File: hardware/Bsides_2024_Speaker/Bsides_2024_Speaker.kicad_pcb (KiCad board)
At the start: 2 copper layers, 144.4 x 144.3 mm, 40 parts, among them J1 Conn_02x03_Odd_Even, J2 Battery, J3 Battery, J4 OLED, P1 USB_C_Plug_USB2.0, Q1 DMG3415U-7, SW1 ON, SW2 RESET, SW3 BOOT, SW4 RESET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

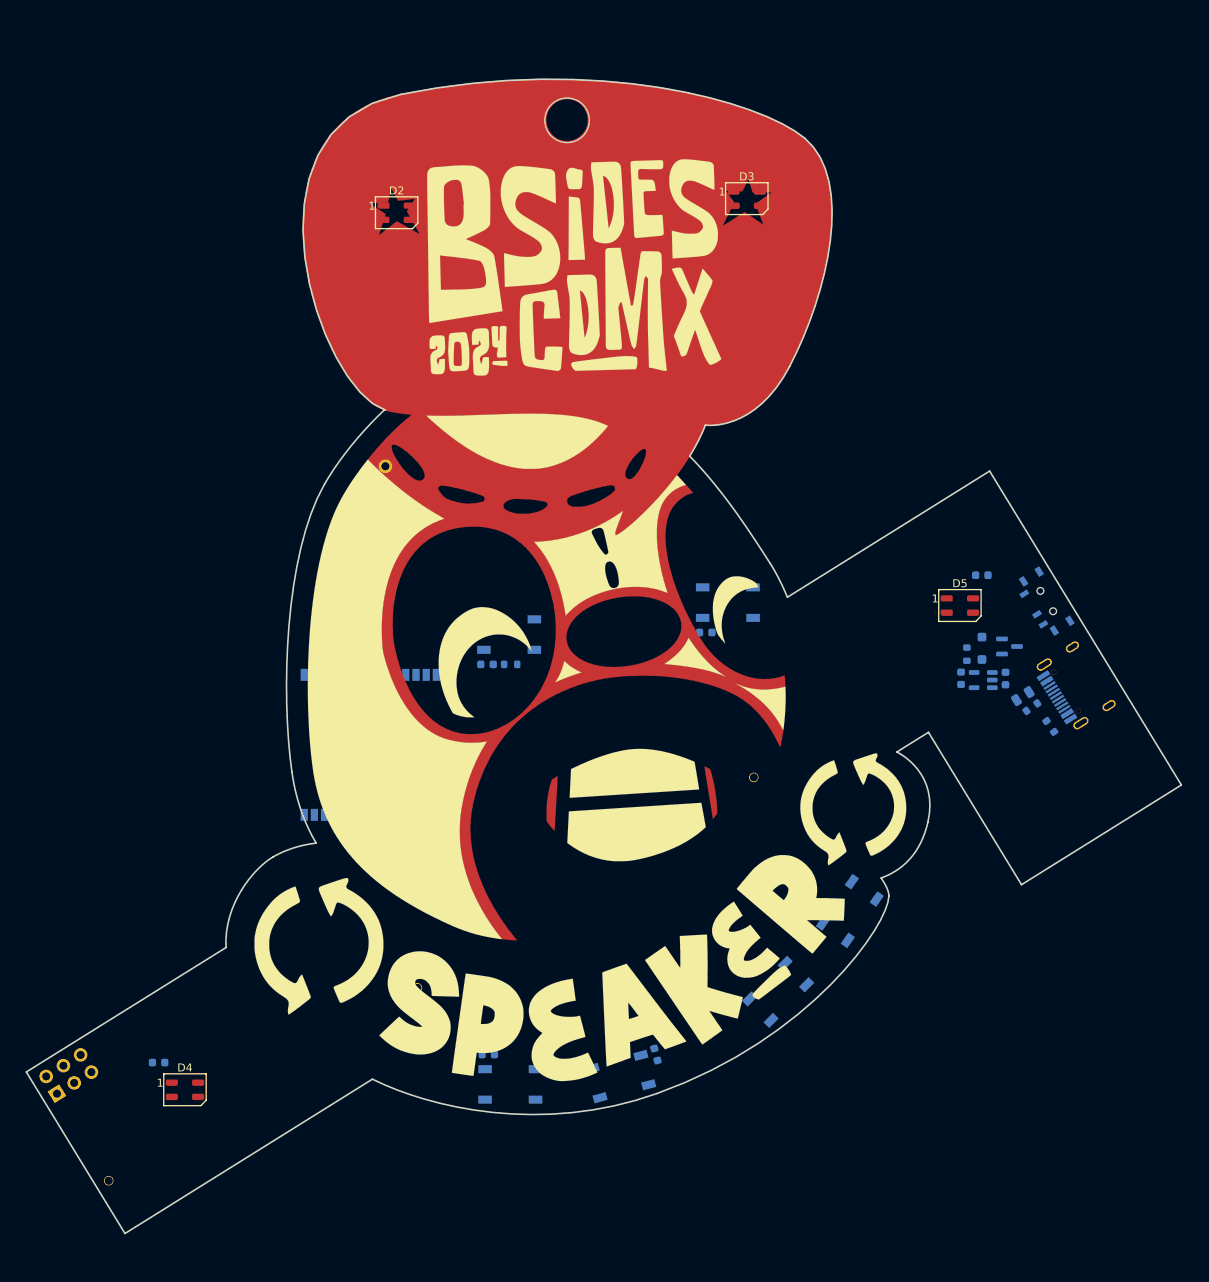
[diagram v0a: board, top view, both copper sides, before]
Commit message: feat(Hw):Update_Route_Speaker
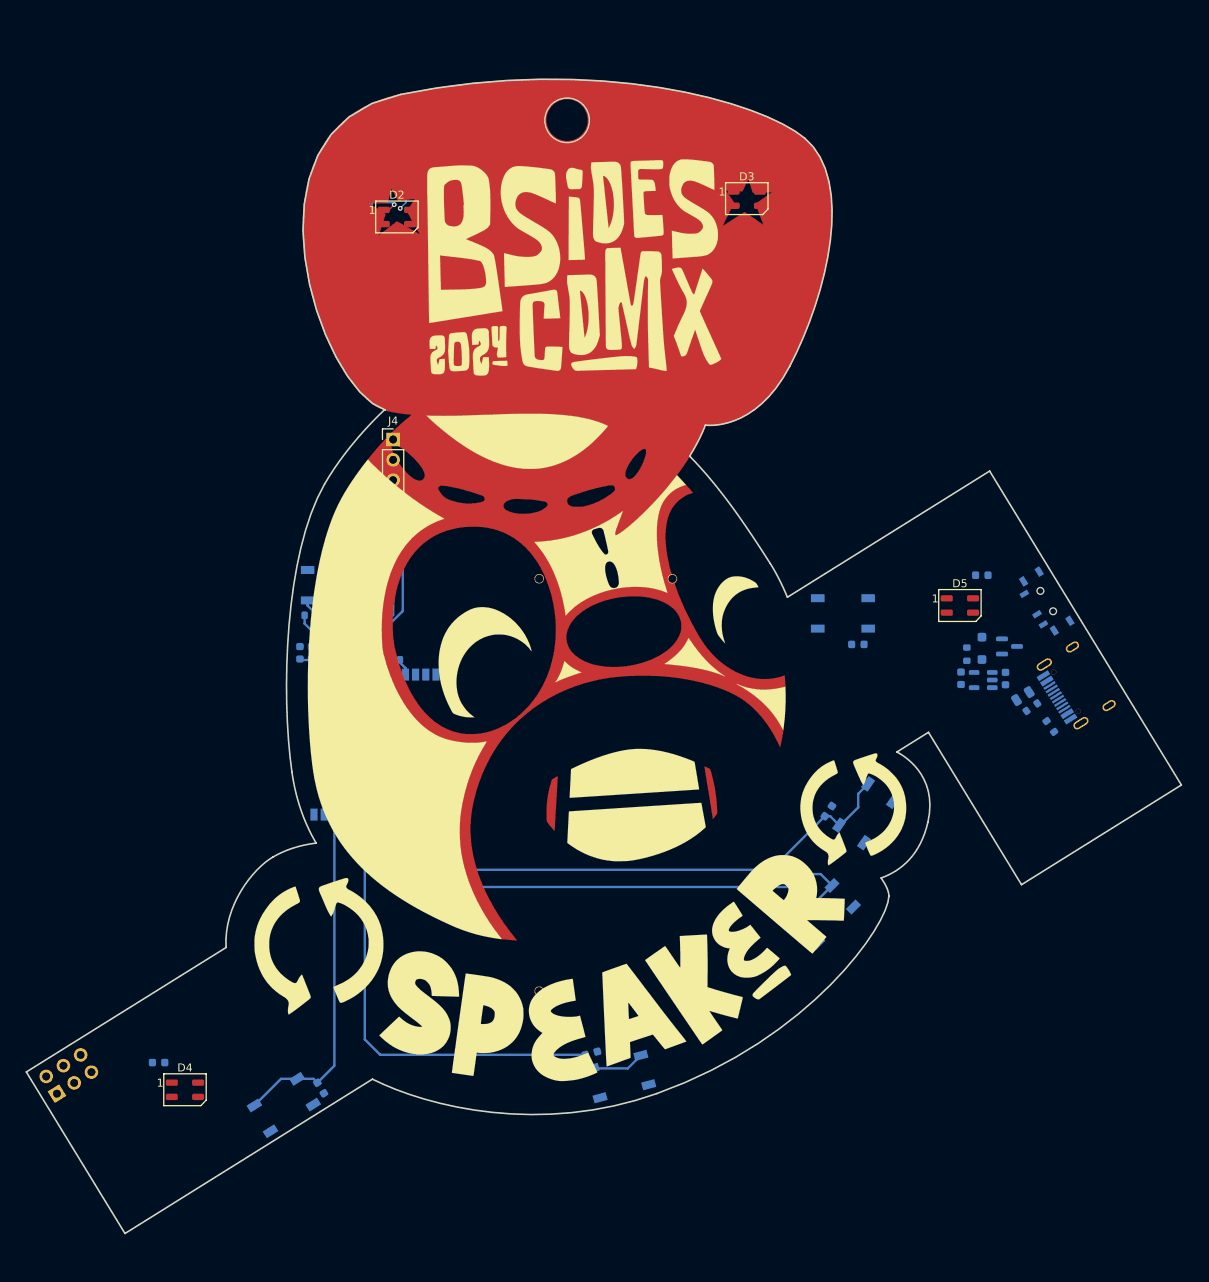
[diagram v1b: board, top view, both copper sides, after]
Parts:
- added C13: 1uF, Capacitor_SMD:C_0603_1608Metric, B.Cu at (111.5, 97.7)
- added C14: 10uF, Capacitor_SMD:C_0603_1608Metric, B.Cu at (108.6, 97.7)
- added C15: 10uF, Capacitor_SMD:C_0603_1608Metric, B.Cu at (110.1, 97.7)
- J2, J3: footprint bsides:BH-AAA-A1aj001 -> bsides:BH-AA-A1AJ020
- J4: moved to F.Cu
- moved J3 50.9 mm to (138.5, 114.2), turned to 90 degrees
- moved SW4 28.4 mm to (106.6, 154.2), turned to 32 degrees
- moved R5 25.7 mm to (110.0, 93.0), turned to 180 degrees
- moved SW2 22.9 mm to (112.7, 89.3)
- moved C8 21.4 mm to (111.2, 152.1), turned to 122 degrees
- moved C4 20.0 mm to (113.0, 93.0), turned to 180 degrees
- moved C3 19.1 mm to (178.3, 96.7)
- moved SW3 14.4 mm to (176.5, 92.8)
- moved J2 14.4 mm to (155.2, 114.2), turned to -90 degrees
- moved SW6 12.4 mm to (179.4, 117.8)
- moved C10 12.4 mm to (174.7, 117.5), turned to -125 degrees
- moved C11 11.4 mm to (170.6, 127.5)
- moved SW7 11.4 mm to (174.2, 130.4)
- moved J4 11.0 mm to (120.2, 71.0)
- moved R1 8.54 mm to (120.3, 98.6)
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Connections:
- C10 pad 2: /GPIO15 -> /GPIO22
- C9 pad 2: /GPIO22 -> /GPIO15
- SW5 pad 2: /GPIO22 -> /GPIO15
- SW6 pad 2: /GPIO15 -> /GPIO22
- U1 pad 26: unconnected-(U1-IO3-Pad26) -> /GPIO1
- U1 pad 9: /GPIO1 -> unconnected-(U1-IO1-Pad9)
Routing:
- net /GPIO22: track 0.00 -> 71.8 mm
- net /GPIO23: track 0.00 -> 71.1 mm
- net /GPIO15: track 0.00 -> 65.3 mm
- net /GPIO1: track 0.00 -> 43.9 mm
- net /SCL: track 0.00 -> 26.2 mm
- net /SDA: track 0.00 -> 23.8 mm
- net +3V3: track 0.00 -> 18.2 mm, vias 0 -> 1
- net /EN: track 0.00 -> 16.0 mm
- net Net-(D2-DIN): track 0.00 -> 2.83 mm, vias 0 -> 1
- net /PIN: track 0.00 -> 2.13 mm

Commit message: feat(Hw):Update_PCB_Speaker
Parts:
- removed the Ref** at (141.8, 92.5)
- added Ref**: Val**, Speaker:Badge_Speaker_Bsides_2024_CDMX, F.Cu at (146.6, 98.3)
- J1: value Conn_02x03_Odd_Even -> Add_On; moved to F.Cu
- moved J1 92.4 mm to (127.0, 74.4), turned to -90 degrees
- moved J4 83.0 mm to (85.5, 146.4)
- moved C8 27.0 mm to (109.5, 125.2)
- moved SW4 25.2 mm to (106.0, 129.1)
- moved R6 6.54 mm to (121.7, 46.1)
- moved C4 4.07 mm to (117.0, 93.0)
- moved C7 2.31 mm to (92.5, 147.3), turned to 180 degrees
- moved C3 1.90 mm to (180.2, 96.6), turned to 180 degrees
- moved J2 1.89 mm to (157.1, 114.1)
- moved R1 1.74 mm to (120.9, 97.0)
- moved SW2 1.68 mm to (114.4, 89.3)
- moved R2 1.10 mm to (191.2, 98.7), turned to 180 degrees
- moved R4 0.95 mm to (202.9, 107.7)
- moved C5 0.81 mm to (117.3, 41.4), turned to -90 degrees
- moved F1 0.75 mm to (199.3, 102.5)
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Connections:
- J1 pad 1: unconnected-(J1-Pin_1-Pad1) -> +3V3
- J1 pad 2: unconnected-(J1-Pin_2-Pad2) -> GND
- J1 pad 3: unconnected-(J1-Pin_3-Pad3) -> /SDA
- J1 pad 4: unconnected-(J1-Pin_4-Pad4) -> /SCL
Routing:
- net +3V3: track 18.2 -> 419.3 mm, vias 1 -> 7
- net Net-(D3-DOUT): track 0.00 -> 173.4 mm, vias 0 -> 2
- net Net-(D4-DOUT): track 0.00 -> 158.0 mm
- net GND: track 0.00 -> 137.0 mm, vias 0 -> 7
- net /SDA: track 23.8 -> 113.8 mm, vias 0 -> 1
- net /SCL: track 26.2 -> 113.4 mm, vias 0 -> 1
- net /D+: track 0.00 -> 87.0 mm
- net /D-: track 0.00 -> 86.8 mm
- net /BOOT: track 0.00 -> 78.6 mm, vias 0 -> 2
- net /PIN: track 2.13 -> 68.0 mm
- net Net-(D2-DOUT): track 0.00 -> 60.3 mm, vias 0 -> 2
- net +BATT: track 0.00 -> 51.1 mm
- net /GPIO1: track 43.9 -> 18.2 mm
- net Net-(SW1-B): track 0.00 -> 21.7 mm, vias 0 -> 2
- net Net-(J2-Pin_1): track 0.00 -> 19.1 mm
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- added copper zone on B.Cu, net GND
- added copper zone on F.Cu, net GND

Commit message: feat:(Hw)Update_PCB_Speaker_Sponsor_Staff
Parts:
- U1: value ESP32-C6-WROOM-1U-N4 -> ESP32-C6-WROOM-1-N4
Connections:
- C1 pad 1: Net-(SW1-B) -> VBUS
- C12 pad 2: +3V3 -> /VOUT
- C13 pad 1: +3V3 -> /VOUT
- C14 pad 1: +3V3 -> /VOUT
- C15 pad 1: +3V3 -> /VOUT
- C2 pad 1: +3V3 -> Net-(D1-A)
- C5 pad 2: +3V3 -> /VOUT
- C6 pad 2: +3V3 -> /VOUT
- C7 pad 2: +3V3 -> /VOUT
- D1 pad 2: VBUS -> Net-(D1-A)
- D2 pad 1: +3V3 -> /VOUT
- D3 pad 1: +3V3 -> /VOUT
- D4 pad 1: +3V3 -> /VOUT
- D5 pad 1: +3V3 -> /VOUT
- J1 pad 1: +3V3 -> /VOUT
- J4 pad 1: +3V3 -> /VOUT
- Q1 pad 1: VBUS -> Net-(D1-A)
- R1 pad 2: +3V3 -> /VOUT
- R2 pad 1: VBUS -> Net-(D1-A)
- R5 pad 2: +3V3 -> /VOUT
- SW1 pad 2: Net-(SW1-B) -> /VOUT
- U1 pad 2: +3V3 -> /VOUT
- U2 pad 1: Net-(SW1-B) -> VBUS
- U2 pad 3: Net-(SW1-B) -> VBUS
- U2 pad 5: +3V3 -> Net-(D1-A)
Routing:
- net +3V3: track 419.3 -> 0.00 mm, vias 7 -> 0
- net /VOUT: track 0.00 -> 411.7 mm, vias 0 -> 6
- net Net-(SW1-B): track 21.7 -> 0.00 mm, vias 2 -> 0
- net GND: track 137.0 -> 119.2 mm
- net Net-(D1-A): track 0.00 -> 8.38 mm
- net VBUS: track 11.7 -> 9.54 mm

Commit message: First_Route_Speaker
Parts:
- added J5: Serial_IN, Connector_PinHeader_2.54mm:PinHeader_1x03_P2.54mm_Vertical, F.Cu at (206.1, 120.0)
- added J6: Serial_OUT, Connector_PinSocket_2.54mm:PinSocket_1x03_P2.54mm_Vertical, B.Cu at (83.6, 161.4)
- moved J1 5.68 mm to (121.9, 71.8), turned to 90 degrees
- moved SW4 0.58 mm to (106.2, 129.6)
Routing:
- net /TX: track 0.00 -> 174.1 mm, vias 0 -> 1
- net /RX: track 0.00 -> 170.7 mm
- net GND: track 119.2 -> 141.4 mm, vias 7 -> 10
- net /VOUT: track 411.7 -> 418.3 mm
- net /SCL: track 113.4 -> 109.5 mm
- net /SDA: track 113.8 -> 115.2 mm

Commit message: feat(Hw): Update schematics
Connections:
- J4 pad 1: /VOUT -> /SDA
- J4 pad 2: GND -> /SCL
- J4 pad 3: /SCL -> /VOUT
- J4 pad 4: /SDA -> GND
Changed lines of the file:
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@@
 			)
 		)
-		(property "manf#" "I2C SH1106 Display Oled Azul 128×64 1.3 ” "
+		(property "manf#" "Display OLED 128×32 0.91 I2C SSD1306 Blanco / Azul"
 			(at 0 0 0)
 			(unlocked yes)
@@
 			(layers "*.Cu" "*.Mask")
 			(remove_unused_layers no)
-			(net 3 "/VOUT")
+			(net 22 "/SDA")
 			(pinfunction "Pin_1")
 			(pintype "passive")
@@
 			(layers "*.Cu" "*.Mask")
 			(remove_unused_layers no)
-			(net 2 "GND")
+			(net 23 "/SCL")
 			(pinfunction "Pin_2")
 			(pintype "passive")
@@
 			(layers "*.Cu" "*.Mask")
 			(remove_unused_layers no)
-			(net 23 "/SCL")
+			(net 3 "/VOUT")
 			(pinfunction "Pin_3")
 			(pintype "passive")
@@
 			(layers "*.Cu" "*.Mask")
 			(remove_unused_layers no)
-			(net 22 "/SDA")
+			(net 2 "GND")
 			(pinfunction "Pin_4")
 			(pintype "passive")
@@
 		)
 		(fp_text user "${REFERENCE}"
-			(at -1.27 2.54 360)
+			(at -1.27 2.54 0)
 			(layer "F.Fab")
 			(effects

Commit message: feat(Hw):Update_Sch_Speaker
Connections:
- J1 pad 5: unconnected-(J1-Pin_5-Pad5) -> /GPIO3
- J1 pad 6: unconnected-(J1-Pin_6-Pad6) -> /GPIO2
- J5 pad 1: /TX -> /GPIO16
- J5 pad 2: /RX -> /GPIO17
- J6 pad 1: /RX -> /GPIO4
- J6 pad 2: /TX -> /GPIO5
- R1 pad 1: /PIN -> Net-(U1-IO8)
- U1 pad 10: /PIN -> Net-(U1-IO8)
- U1 pad 11: unconnected-(U1-IO10-Pad11) -> /PIN
- U1 pad 24: /RX -> /GPIO17
- U1 pad 25: /TX -> /GPIO16
- U1 pad 26: /GPIO1 -> /GPIO3
- U1 pad 27: unconnected-(U1-IO2-Pad27) -> /GPIO2
- U1 pad 4: unconnected-(U1-IO4-Pad4) -> /GPIO4
- U1 pad 5: unconnected-(U1-IO5-Pad5) -> /GPIO5
- U1 pad 9: unconnected-(U1-IO1-Pad9) -> /GPIO1
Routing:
- net /TX: track 174.1 -> 0.00 mm, vias 1 -> 0
- net /RX: track 170.7 -> 0.00 mm
- net /GPIO16: track 0.00 -> 106.9 mm, vias 0 -> 1
- net /GPIO17: track 0.00 -> 103.4 mm
- net /GPIO5: track 0.00 -> 87.1 mm, vias 0 -> 1
- net /GPIO4: track 0.00 -> 84.6 mm, vias 0 -> 2
- net /GPIO1: track 18.5 -> 42.9 mm, vias 0 -> 2
- net /GPIO3: track 0.00 -> 15.9 mm
- net GND: track 141.4 -> 125.6 mm
- net /SDA: track 115.2 -> 108.5 mm
- net Net-(U1-IO8): track 0.00 -> 3.47 mm
- net /VOUT: track 418.3 -> 421.1 mm
- net /SCL: track 109.5 -> 107.1 mm
- net /PIN: track 68.0 -> 67.2 mm

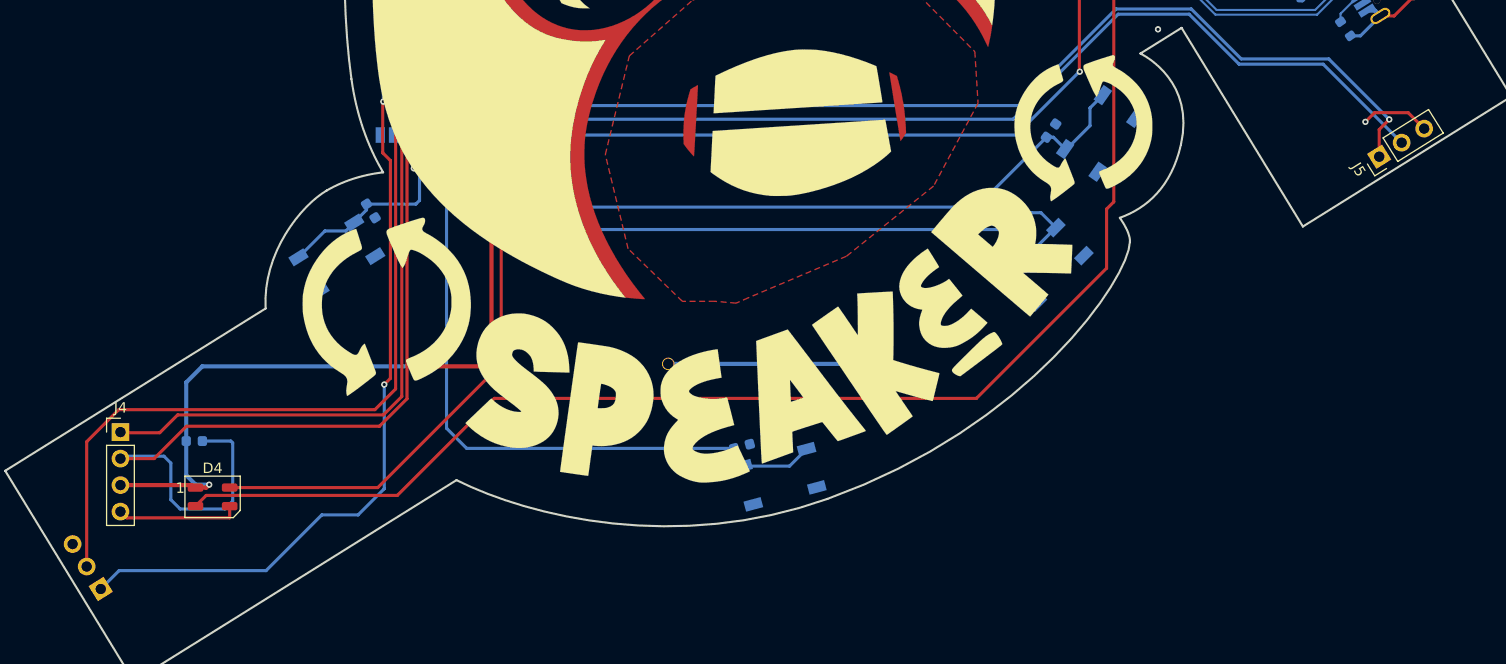
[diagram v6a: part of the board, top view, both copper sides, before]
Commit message: feat(Hw):Update_Staff_Sch_And_PCB
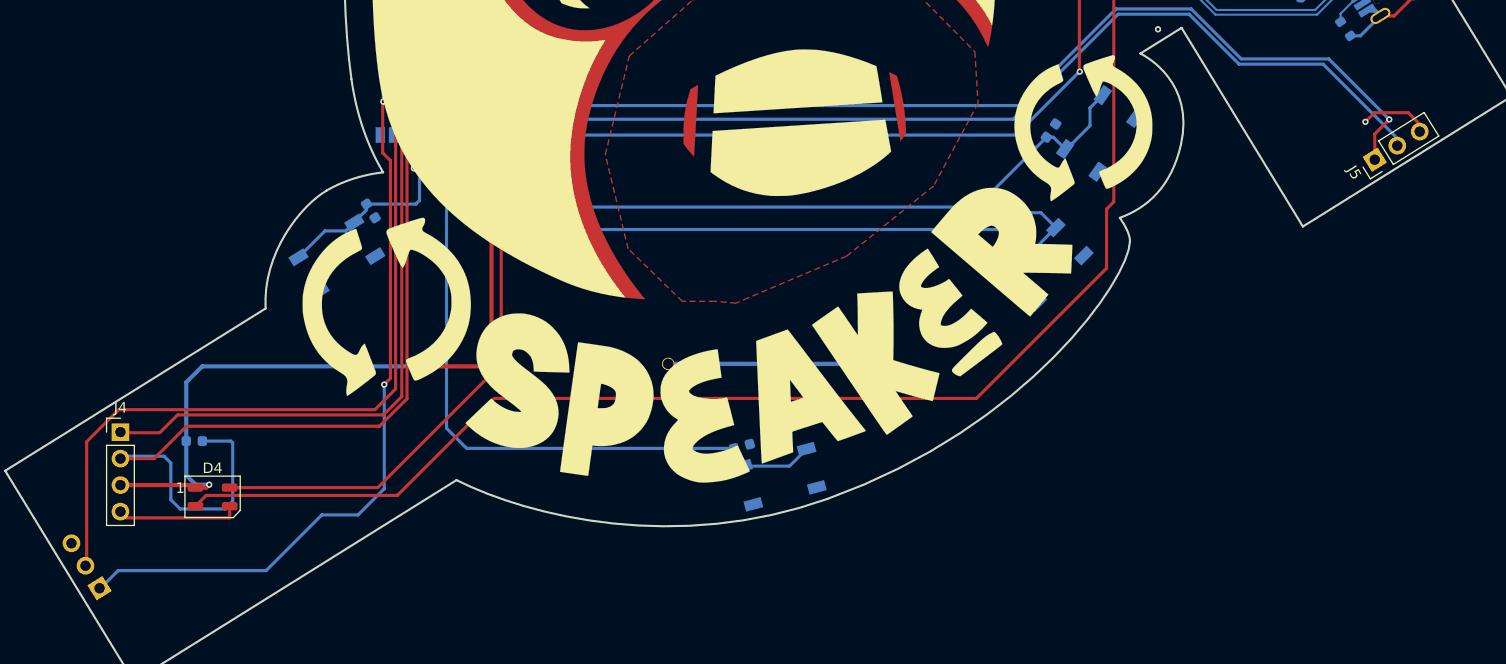
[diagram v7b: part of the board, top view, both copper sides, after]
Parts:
- moved J5 0.51 mm to (205.7, 120.3)
- moved J6 0.14 mm to (83.4, 161.4)
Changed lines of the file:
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@@
 	(footprint "Connector_PinHeader_2.54mm:PinHeader_1x03_P2.54mm_Vertical"
 		(layer "F.Cu")
-		(at 206.111916 120.001989 122)
+		(at 205.69 120.29 122)
 		(descr "Through hole straight pin header, 1x03, 2.54mm pitch, single row")
 		(tags "Through hole pin header THT 1x03 2.54mm single row")
@@
 	(footprint "Connector_PinSocket_2.54mm:PinSocket_1x03_P2.54mm_Vertical"
 		(layer "B.Cu")
-		(at 83.56 161.44 32)
+		(at 83.445995 161.364042 32)
 		(descr "Through hole straight socket strip, 1x03, 2.54mm pitch, single row (from Kicad 4.0.7), script generated")
 		(tags "Through hole socket strip THT 1x03 2.54mm single row")
@@
 	)
 	(segment
-		(start 110.74 151.83)
-		(end 108.23 154.34)
-		(width 0.3)
-		(layer "B.Cu")
-		(net 29)
-	)
-	(segment
 		(start 111.19 111.38)
 		(end 111.19 105.11)
@@
 	)
 	(segment
-		(start 108.23 154.34)
-		(end 104.75 154.34)
+		(start 104.75 154.34)
+		(end 99.41 159.68)
 		(width 0.3)
 		(layer "B.Cu")
@@
 	)
 	(segment
-		(start 111.19 105.11)
-		(end 114.17 102.13)
+		(start 110.74 151.83)
+		(end 108.23 154.34)
 		(width 0.3)
 		(layer "B.Cu")
@@
 	)
 	(segment
-		(start 99.41 159.68)
-		(end 85.32 159.68)
+		(start 111.19 105.11)
+		(end 114.17 102.13)
 		(width 0.3)
 		(layer "B.Cu")
@@
 	)
 	(segment
-		(start 110.74 141.84)
-		(end 110.74 151.83)
+		(start 108.23 154.34)
+		(end 104.75 154.34)
 		(width 0.3)
 		(layer "B.Cu")
@@
 	)
 	(segment
-		(start 104.75 154.34)
-		(end 99.41 159.68)
+		(start 85.22 159.68)
+		(end 83.49 161.41)
 		(width 0.3)
 		(layer "B.Cu")
@@
 	)
 	(segment
-		(start 85.32 159.68)
-		(end 83.56 161.44)
+		(start 99.41 159.68)
+		(end 85.22 159.68)
 		(width 0.3)
 		(layer "B.Cu")
@@
 	)
 	(segment
+		(start 110.74 141.84)
+		(end 110.74 151.83)
+		(width 0.3)
+		(layer "B.Cu")
+		(net 29)
+	)
+	(segment
 		(start 111.828435 113.681565)
 		(end 111.828435 142.261565)
@@
 	)
 	(segment
+		(start 82.214005 159.185958)
+		(end 82.144005 159.255958)
+		(width 0.3)
+		(layer "F.Cu")
+		(net 30)
+	)
+	(segment
 		(start 111.84 113.67)
 		(end 111.828435 113.681565)
@@
 	)
 	(segment
-		(start 85.288553 144.251447)
-		(end 82.214005 147.325995)
+		(start 111.828435 142.261565)
+		(end 109.838553 144.251447)
 		(width 0.3)
 		(layer "F.Cu")
@@
 	(segment
 		(start 82.214005 147.325995)
-		(end 82.214005 159.285958)
+		(end 82.214005 159.185958)
 		(width 0.3)
 		(layer "F.Cu")
@@
 	)
 	(segment
-		(start 111.828435 142.261565)
-		(end 109.838553 144.251447)
+		(start 85.288553 144.251447)
+		(end 82.214005 147.325995)
 		(width 0.3)
 		(layer "F.Cu")
@@
 	)
 	(segment
-		(start 115.76 116.41)
-		(end 115.44 116.73)
+		(start 181.09 106.34)
+		(end 171.02 116.41)
 		(width 0.3)
 		(layer "B.Cu")
@@
 	)
 	(segment
-		(start 187.892894 106.34)
-		(end 181.09 106.34)
+		(start 171.02 116.41)
+		(end 115.76 116.41)
 		(width 0.3)
 		(layer "B.Cu")
@@
 	)
 	(segment
-		(start 181.09 106.34)
-		(end 171.02 116.41)
+		(start 115.76 116.41)
+		(end 115.44 116.73)
 		(width 0.3)
 		(layer "B.Cu")
@@
 	)
 	(segment
-		(start 200.739963 111.13)
-		(end 192.682894 111.13)
+		(start 187.892894 106.34)
+		(end 181.09 106.34)
 		(width 0.3)
 		(layer "B.Cu")
@@
 	)
 	(segment
-		(start 115.44 116.73)
-		(end 115.44 117.925)
+		(start 207.844041 118.944005)
+		(end 207.844041 118.234078)
 		(width 0.3)
 		(layer "B.Cu")
@@
 	)
 	(segment
-		(start 208.265957 118.655994)
+		(start 200.739963 111.13)
+		(end 192.682894 111.13)
+		(width 0.3)
+		(layer "B.Cu")
+		(net 32)
+	)
+	(segment
+		(start 207.844041 118.234078)
 		(end 200.739963 111.13)
 		(width 0.3)
@@
 	)
 	(segment
-		(start 171.02 116.41)
-		(end 115.76 116.41)
+		(start 115.44 116.73)
+		(end 115.44 117.925)
 		(width 0.3)
 		(layer "B.Cu")
@@
 	)
 	(segment
-		(start 206.111916 117.398084)
-		(end 206.111916 120.001989)
+		(start 207.08 116.43)
+		(end 205.69 117.82)
 		(width 0.3)
 		(layer "F.Cu")
@@
 	)
 	(segment
-		(start 207.08 116.43)
-		(end 206.111916 117.398084)
+		(start 205.69 117.82)
+		(end 205.69 120.29)
 		(width 0.3)
 		(layer "F.Cu")

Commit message: feat(Hw):First_Route_Staff
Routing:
- net /GPIO2: track 0.00 -> 54.4 mm, vias 0 -> 1
- net /GPIO3: track 15.9 -> 59.3 mm, vias 0 -> 1
- net Net-(D3-DOUT): track 173.4 -> 180.7 mm
- net GND: track 125.6 -> 132.7 mm, vias 10 -> 11
